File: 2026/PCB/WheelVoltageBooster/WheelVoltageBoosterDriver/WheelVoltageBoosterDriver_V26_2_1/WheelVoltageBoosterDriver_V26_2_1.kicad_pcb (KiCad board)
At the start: 2 copper layers, 100 x 65 mm, 232 parts, among them J1 Conn_01x02_Pin, J10 Conn_01x03_Socket, J11 Conn_01x05_Socket, J13 Conn_01x04_Socket, J2 Conn_01x02_Pin, J3 Conn_01x04_Socket, J4 Conn_01x04_Socket, J5 Conn_01x04_Socket, J6 Conn_01x04_Socket, J7 Conn_01x02_Pin, J8 Conn_01x07_Socket, J9 Conn_01x03_Socket, SW1 SW_MEC_5E, SW2 SW_MEC_5E, U1 MAX3051, U2 LM5170QPHPTQ1, U3 STM32H523CEU6, U4 TMP235AQDCKRQ1, U5 MAX20405AFOA/VY+, U6 MCP1703AT-3302E/CB, U7 MAX20405AFOA/VY+, Y1 Crystal_GND2

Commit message: FTP割り当て完了
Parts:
- removed C100, C101, C102, C103, C104, C105, C106, C107, C60, C61, C62, C80, C81, C82, C83, C84, C85, C86, C87, C88, C89, C90, C91, C92, C93, C94, C95, C96, C97, C98, C99: 10u, Capacitor_SMD:C_1210_3225Metric_Pad1.33x2.70mm_HandSolder
- removed D11, D12, D8: LED, WheelVoltageBooster_LIB_FTP:LED_1608_user_dif
- removed D13, D14: SMAJ26A, WheelVoltageBooster_LIB_FTP:D_SMA_UD
- removed FET11, FET12, FET13, FET14: FDMS86183, WheelVoltageBooster_LIB_FTP:PQFN-8-EP_6x5mm_P1.27mm_Generic_ud
- removed J6: Conn_01x04_Socket, WheelVoltageBooster_LIB_FTP:PinSocket_1x04_P2.54mm_Vertical_ud
- removed R41, R42: 1m, Resistor_SMD:R_2512_6332Metric
- removed R45, R46, R49, R50, R53, R54, R55, R56: 50k, Resistor_SMD:R_0402_1005Metric_Pad0.72x0.64mm_HandSolder
- removed REF** (x4): hole_M3_User, WheelVoltageBooster_LIB_FTP:hole_M3_User
- removed REF** (x4): MountingHole_2.2mm_M2_Pad_Via, MountingHole:MountingHole_2.2mm_M2_Pad_Via
- removed REF**: Symbol_HighVoltage_Triangle_6x6mm_Copper, Symbol:Symbol_HighVoltage_Triangle_6x6mm_Copper
- added R16: 50k, Resistor_SMD:R_0603_1608Metric_Pad0.98x0.95mm_HandSolder, F.Cu at (142.4, 50.9)
- added U10: HIP2101EIBZT, Package_SO:SOIC-8-1EP_3.9x4.9mm_P1.27mm_EP2.514x3.2mm, F.Cu at (141.8, 83.3)
- added U8: MAX15158A, Package_DFN_QFN:TQFN-32-1EP_5x5mm_P0.5mm_EP3.1x3.1mm, F.Cu at (150.3, 83.3)
- added U9: HIP2101EIBZT, Package_SO:SOIC-8-1EP_3.9x4.9mm_P1.27mm_EP2.514x3.2mm, F.Cu at (158.6, 83.1)
- C10: value 10n -> 10u; footprint Capacitor_SMD:C_0603_1608Metric_Pad1.08x0.95mm_HandSolder -> Capacitor_SMD:C_1210_3225Metric_Pad1.33x2.70mm_HandSolder
- C11, C13: value 9n -> 1n
- C16: value 10n -> 68u; footprint Capacitor_SMD:C_0603_1608Metric_Pad1.08x0.95mm_HandSolder -> WheelVoltageBooster_LIB_FTP:CAP_EEEFN1K470UP
- C27, C29, C31: value 220u -> 10u; footprint WheelVoltageBooster_LIB_FTP:CAP_EEEFN1H181UP -> Capacitor_SMD:C_1210_3225Metric_Pad1.33x2.70mm_HandSolder
- C28, C30, C35, C37: value 10u -> 68u; footprint Capacitor_SMD:C_1210_3225Metric_Pad1.33x2.70mm_HandSolder -> WheelVoltageBooster_LIB_FTP:CAP_EEEFN1K470UP; moved to F.Cu
- C3: value 1n -> 2.2u
- C32, C50: value 10u -> 1n; footprint Capacitor_SMD:C_1210_3225Metric_Pad1.33x2.70mm_HandSolder -> Capacitor_SMD:C_0603_1608Metric_Pad1.08x0.95mm_HandSolder
- C33: value 220u -> 68u; footprint WheelVoltageBooster_LIB_FTP:CAP_EEEFN1H181UP -> WheelVoltageBooster_LIB_FTP:CAP_EEEFN1K470UP
- C39: value 220n -> 68u; footprint Capacitor_SMD:C_0603_1608Metric_Pad1.08x0.95mm_HandSolder -> WheelVoltageBooster_LIB_FTP:CAP_EEEFN1K470UP
- C4: value 1n -> 47n
- C40: value 220n -> 10u; footprint Capacitor_SMD:C_0603_1608Metric_Pad1.08x0.95mm_HandSolder -> Capacitor_SMD:C_1210_3225Metric_Pad1.33x2.70mm_HandSolder
- C45, C47, C51, C53: value 68u -> 220u; footprint WheelVoltageBooster_LIB_FTP:CAP_EEEFN1K470UP -> WheelVoltageBooster_LIB_FTP:CAP_EEEFN1H181UP
- C49, C55: value 68u -> 1n; footprint WheelVoltageBooster_LIB_FTP:CAP_EEEFN1K470UP -> Capacitor_SMD:C_0603_1608Metric_Pad1.08x0.95mm_HandSolder
- C5: value 1u -> 73n
- C56, C58: value 10u -> 220u; footprint Capacitor_SMD:C_1210_3225Metric_Pad1.33x2.70mm_HandSolder -> WheelVoltageBooster_LIB_FTP:CAP_EEEFN1H181UP
- C57, C59: value 68u -> 10u; footprint WheelVoltageBooster_LIB_FTP:CAP_EEEFN1K470UP -> Capacitor_SMD:C_1210_3225Metric_Pad1.33x2.70mm_HandSolder
- C6: value 500p -> 73p
- C7: value 500p -> 0.1u
- C8: value 47n -> 0.1u
- C9: value 47n -> 68u; footprint Capacitor_SMD:C_0603_1608Metric_Pad1.08x0.95mm_HandSolder -> WheelVoltageBooster_LIB_FTP:CAP_EEEFN1K470UP
- D1, D2: value SMAJ12A -> LED; footprint WheelVoltageBooster_LIB_FTP:D_SMA_UD -> WheelVoltageBooster_LIB_FTP:LED_1608_user_dif
- J1: value Conn_01x02_Pin -> Conn_01x04_Socket; footprint WheelVoltageBooster_LIB_FTP:AMASS_XT30PW-M_1x02_P2.50mm_Horizontal_ud -> Connector_PinSocket_2.54mm:PinSocket_1x04_P2.54mm_Vertical
- J3, J4, J5: footprint WheelVoltageBooster_LIB_FTP:PinSocket_1x04_P2.54mm_Vertical_ud -> Connector_PinSocket_2.54mm:PinSocket_1x04_P2.54mm_Vertical
- R1: value 2.4k -> 3k; footprint Resistor_SMD:R_0603_1608Metric_Pad0.98x0.95mm_HandSolder -> Resistor_SMD:R_0402_1005Metric_Pad0.72x0.64mm_HandSolder
- R10: value 43k -> 2k; footprint Resistor_SMD:R_0603_1608Metric_Pad0.98x0.95mm_HandSolder -> Resistor_SMD:R_0402_1005Metric_Pad0.72x0.64mm_HandSolder
- R11: value 21k -> 7.2k; footprint Resistor_SMD:R_0603_1608Metric_Pad0.98x0.95mm_HandSolder -> Resistor_SMD:R_0402_1005Metric_Pad0.72x0.64mm_HandSolder
- R14: value 11k -> 50k
- R17: value 11k -> 1k
- R2: value 2.4k -> 1k; footprint Resistor_SMD:R_0603_1608Metric_Pad0.98x0.95mm_HandSolder -> Resistor_SMD:R_0402_1005Metric_Pad0.72x0.64mm_HandSolder
- R3: value 25 -> 3k; footprint Resistor_SMD:R_0603_1608Metric_Pad0.98x0.95mm_HandSolder -> Resistor_SMD:R_0402_1005Metric_Pad0.72x0.64mm_HandSolder
- R31, R32: value 1k -> 10; footprint Resistor_SMD:R_0603_1608Metric_Pad0.98x0.95mm_HandSolder -> Resistor_SMD:R_01005_0402Metric_Pad0.57x0.30mm_HandSolder
- R36: value 50k -> 3m
- R37: value 50k -> 10; footprint Resistor_SMD:R_0603_1608Metric_Pad0.98x0.95mm_HandSolder -> Resistor_SMD:R_01005_0402Metric_Pad0.57x0.30mm_HandSolder
- R38: value 1M -> 10; footprint Resistor_SMD:R_0402_1005Metric_Pad0.72x0.64mm_HandSolder -> Resistor_SMD:R_01005_0402Metric_Pad0.57x0.30mm_HandSolder
- R4: value 24k -> 1k; footprint Resistor_SMD:R_0603_1608Metric_Pad0.98x0.95mm_HandSolder -> Resistor_SMD:R_0402_1005Metric_Pad0.72x0.64mm_HandSolder
- R5: value 24k -> 100k; footprint Resistor_SMD:R_0603_1608Metric_Pad0.98x0.95mm_HandSolder -> Resistor_SMD:R_0402_1005Metric_Pad0.72x0.64mm_HandSolder
- R6: value 10k -> 35k; footprint Resistor_SMD:R_0603_1608Metric_Pad0.98x0.95mm_HandSolder -> Resistor_SMD:R_0402_1005Metric_Pad0.72x0.64mm_HandSolder
- R7: value 10k -> 60k; footprint Resistor_SMD:R_0603_1608Metric_Pad0.98x0.95mm_HandSolder -> Resistor_SMD:R_0402_1005Metric_Pad0.72x0.64mm_HandSolder
- R8: value 10k -> 100k; footprint Resistor_SMD:R_0603_1608Metric_Pad0.98x0.95mm_HandSolder -> Resistor_SMD:R_0402_1005Metric_Pad0.72x0.64mm_HandSolder
- R9: value 65k -> 48k; footprint Resistor_SMD:R_0603_1608Metric_Pad0.98x0.95mm_HandSolder -> Resistor_SMD:R_0402_1005Metric_Pad0.72x0.64mm_HandSolder
- U2: value LM5170QPHPTQ1 -> TMP235AQDCKRQ1; footprint WheelVoltageBooster_LIB_FTP:LM5170QPHPTQ1 -> Package_TO_SOT_SMD:SOT-353_SC-70-5
- Y1: value Crystal_GND2 -> CSTNE16M0V530000R0
- moved C53 58.4 mm to (90.3, 51.6)
- moved C10 57.1 mm to (183.3, 48.0)
- moved C3 57.1 mm to (198.1, 45.7)
- moved C5 57.1 mm to (198.1, 42.7)
- moved C6 57.1 mm to (201.6, 45.7)
- moved C8 57.1 mm to (201.6, 44.2)
- moved R1 57.1 mm to (201.6, 42.7)
- moved R10 57.1 mm to (194.5, 48.0)
- moved R11 57.1 mm to (198.1, 41.2)
- moved R3 57.1 mm to (201.6, 41.2)
- moved R4 57.1 mm to (198.1, 44.2)
- moved C14 57.1 mm to (198.1, 38.1)
- moved C19 57.1 mm to (201.6, 38.1)
- moved C24 57.1 mm to (188.9, 58.3)
- moved D1 57.1 mm to (199.9, 48.3)
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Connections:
- net +6V5 renamed 6V5
- C1 pad 1: +3V3 -> 3V3
- C10 pad 1: GND -> 50V
- C10 pad 2: Net-(U2-SS) -> GND
- C11 pad 1: IOUT1 -> CSP1
- C13 pad 1: IOUT2 -> CSN1
- C14 pad 2: +3V3 -> 3V3
- C15 pad 2: +3V3 -> 3V3
- C16 pad 1: GND -> 50V
- C16 pad 2: Net-(U2-ISETA) -> GND
- C17 pad 2: +3V3 -> 3V3
- C18 pad 2: +3V3 -> 3V3
- C19 pad 2: +3V3 -> 3V3
- C2 pad 1: GND -> 3V3
- C2 pad 2: +10V -> GND
- C20 pad 1: +3V3 -> 3V3
- C22 pad 1: +3V3 -> 3V3
- C24 pad 1: +3V3 -> 3V3
- C27 pad 1: +20V -> 50V
- C28 pad 1: +20V -> 50V
- C29 pad 1: +20V -> 50V
- C3 pad 2: Net-(U2-RAMP1) -> Net-(U8-BIAS)
- C30 pad 1: +20V -> 50V
- C31 pad 1: +20V -> 50V
- C32 pad 1: +20V -> CSP1
- C32 pad 2: GND -> CSN1
- C33 pad 1: +20V -> 50V
- C34 pad 1: +20V -> 50V
- C35 pad 1: +20V -> 50V
- C36 pad 1: +20V -> 50V
- C37 pad 1: +20V -> 50V
- C38 pad 1: +20V -> 50V
- C39 pad 1: /Power_Circuit/SW2 -> 50V
- C39 pad 2: /Power_Circuit/HB2 -> GND
- C4 pad 1: GND -> Net-(U8-SS)
- C4 pad 2: Net-(U2-RAMP2) -> GND
- C40 pad 1: /Power_Circuit/SW1 -> 50V
- C40 pad 2: /Power_Circuit/HB1 -> GND
- C41 pad 1: +50V -> 50V
- C42 pad 1: +50V -> 50V
- C43 pad 1: +50V -> 50V
- C44 pad 1: +50V -> 50V
- C45 pad 1: +50V -> 25V
- C46 pad 1: +20V -> 25V
- C47 pad 1: +50V -> 25V
- C48 pad 1: +20V -> 25V
- C49 pad 1: +50V -> CSP2
- C5 pad 1: GND -> Net-(C5-Pad1)
- C5 pad 2: Net-(U2-OPT) -> GND
- C50 pad 1: +50V -> CSN2
- C51 pad 1: +50V -> 25V
- C52 pad 1: +50V -> 25V
- C53 pad 1: +50V -> 25V
- C54 pad 1: +50V -> 25V
- C55 pad 1: +50V -> CSP2
- C55 pad 2: GND -> CSN2
- C56 pad 1: +50V -> 25V
- C57 pad 1: +50V -> 25V
- C58 pad 1: +50V -> 25V
- C59 pad 1: +50V -> 25V
- C6 pad 1: GND -> COMP
- C6 pad 2: Net-(U2-COMP1) -> GND
- C64 pad 1: +20V -> 25V
- C65 pad 1: +20V -> 25V
- C7 pad 1: GND -> Net-(U9-HB)
- C7 pad 2: Net-(U2-COMP2) -> HS1
- C72 pad 1: +3V3 -> 3V3
- C73 pad 1: +20V -> 25V
- C74 pad 1: +20V -> 25V
- C77 pad 1: +10V -> 10V
- C78 pad 1: +10V -> 10V
- C79 pad 1: +10V -> 10V
- C8 pad 1: Net-(C8-Pad1) -> Net-(U10-HB)
- C8 pad 2: Net-(U2-COMP1) -> HS2
- C9 pad 1: Net-(C9-Pad1) -> 50V
- C9 pad 2: Net-(U2-COMP2) -> GND
- D1 pad 1: /Power_Circuit/HB1 -> GND
- D1 pad 2: +10V -> Net-(D1-A)
- D2 pad 1: /Power_Circuit/HB2 -> GND
- D2 pad 2: +10V -> Net-(D2-A)
- FET10 pad 1: GND -> SR2
- FET10 pad 2: GND -> SR2
- FET10 pad 3: GND -> SR2
- FET10 pad 4: /Power_Circuit/LO1 -> LO2
- FET10 pad 5: /Power_Circuit/SW1 -> HS2
- FET3 pad 1: /Power_Circuit/BRKS -> HS1
- FET3 pad 2: /Power_Circuit/BRKS -> HS1
- FET3 pad 3: /Power_Circuit/BRKS -> HS1
- FET3 pad 4: /Power_Circuit/BRKG -> HO1
- FET3 pad 5: +20V -> 50V
- FET4 pad 1: /Power_Circuit/BRKS -> SR1
- FET4 pad 2: /Power_Circuit/BRKS -> SR1
- FET4 pad 3: /Power_Circuit/BRKS -> SR1
- FET4 pad 4: /Power_Circuit/BRKG -> LO1
- FET4 pad 5: +20V -> HS1
- FET5 pad 1: /Power_Circuit/BRKS -> HS1
- FET5 pad 2: /Power_Circuit/BRKS -> HS1
- FET5 pad 3: /Power_Circuit/BRKS -> HS1
- FET5 pad 4: /Power_Circuit/BRKG -> HO1
- FET5 pad 5: /Power_Circuit/CS1B -> 50V
- FET6 pad 1: /Power_Circuit/BRKS -> SR1
- FET6 pad 2: /Power_Circuit/BRKS -> SR1
- FET6 pad 3: /Power_Circuit/BRKS -> SR1
- FET6 pad 4: /Power_Circuit/BRKG -> LO1
- FET6 pad 5: /Power_Circuit/CS1B -> HS1
- FET7 pad 1: GND -> HS2
- FET7 pad 2: GND -> HS2
- FET7 pad 3: GND -> HS2
- FET7 pad 4: /Power_Circuit/LO2 -> HO2
- FET7 pad 5: /Power_Circuit/SW2 -> 50V
- FET8 pad 1: GND -> SR2
- FET8 pad 2: GND -> SR2
- FET8 pad 3: GND -> SR2
- FET8 pad 4: /Power_Circuit/LO1 -> LO2
- FET8 pad 5: /Power_Circuit/SW1 -> HS2
- FET9 pad 1: GND -> HS2
- FET9 pad 2: GND -> HS2
- FET9 pad 3: GND -> HS2
- FET9 pad 4: /Power_Circuit/LO2 -> HO2
- FET9 pad 5: /Power_Circuit/SW2 -> 50V
- J1 pad 1: GND -> 50V
- J1 pad 2: +20V -> 50V
- J10 pad 1: +3V3 -> 3V3
- J10 pad 2: +3V3 -> 3V3
- J10 pad 3: +3V3 -> 3V3
- J11 pad 2: +20V -> 25V
- J13 pad 2: +20V -> 25V
- J2 pad 1: +20V -> 25V
- J3 pad 1: +50V -> 50V
- J3 pad 2: +50V -> 50V
- J3 pad 3: +50V -> 50V
- J3 pad 4: +50V -> 50V
- J4 pad 1: +50V -> GND
- J4 pad 2: +50V -> GND
- J4 pad 3: +50V -> GND
- J4 pad 4: +50V -> GND
- J7 pad 1: +20V -> 25V
- J8 pad 6: +3V3 -> 3V3
- J9 pad 1: +3V3 -> 3V3
- J9 pad 2: +3V3 -> 3V3
- J9 pad 3: +3V3 -> 3V3
- L1 pad 1: /Power_Circuit/CS2A -> 25V
- L1 pad 2: /Power_Circuit/SW2 -> HS1
- L1 pad 3: GND -> (no net)
- L2 pad 1: /Power_Circuit/CS1A -> 25V
- L2 pad 2: /Power_Circuit/SW1 -> HS2
- L2 pad 3: GND -> (no net)
- L4 pad 2: +10V -> 10V
- R1 pad 1: GND -> LO1
- R1 pad 2: Net-(C8-Pad1) -> DLFB1
- R10 pad 1: GND -> FB
- R10 pad 2: Net-(U2-OVPB) -> GND
- R11 pad 1: GND -> COMP
- R11 pad 2: Net-(U2-IPK) -> Net-(C5-Pad1)
- R14 pad 1: IOUT1 -> 50V
- R14 pad 2: GND -> Net-(D1-A)
- R15 pad 1: +20V -> 25V
- R17 pad 1: IOUT2 -> /Power_Circuit/MREN
- R17 pad 2: GND -> Net-(D7-A)
- R2 pad 1: GND -> DLFB1
- R2 pad 2: Net-(C9-Pad1) -> GND
- R22 pad 1: +50V -> 50V
- R22 pad 2: VM_SCAN2 -> /Power_Circuit/MRVFB1
- R23 pad 1: VM_SCAN2 -> /Power_Circuit/MRVFB1
- R24 pad 1: +50V -> 50V
- R24 pad 2: VM_SCAN1 -> /Power_Circuit/MRVFB2
- R25 pad 1: VM_SCAN1 -> /Power_Circuit/MRVFB2
- R26 pad 1: +3V3 -> 3V3
- R3 pad 1: +10V -> LO2
- R3 pad 2: Net-(U2-OPT) -> DLFB2
- R31 pad 1: EN1 -> CSP1
- R31 pad 2: Net-(D7-A) -> SR1
- R32 pad 1: EN2 -> CSN1
- R32 pad 2: Net-(D8-A) -> GND
- R35 pad 1: +3V3 -> 3V3
- R36 pad 1: +50V -> SR1
- R36 pad 2: Net-(D11-A) -> GND
- R37 pad 1: +50V -> CSP2
- R37 pad 2: Net-(D12-A) -> SR2
- R38 pad 1: /Power_Circuit/BRKG -> CSN2
- R38 pad 2: /Power_Circuit/BRKS -> GND
- R4 pad 1: Net-(U2-VINX) -> DLFB2
- R4 pad 2: Net-(U2-RAMP1) -> GND
- R5 pad 1: Net-(U2-VINX) -> Net-(U8-BIAS)
- R5 pad 2: Net-(U2-RAMP2) -> /Power_Circuit/PGOOD
- R6 pad 2: Net-(U2-OSC) -> Net-(U8-RAMP)
- R61 pad 1: +20V -> 25V
- R62 pad 1: +10V -> 10V
- R64 pad 1: +3V3 -> 3V3
- R68 pad 2: +10V -> 10V
- R7 pad 2: Net-(U2-SYNCOUT) -> Net-(U8-ILIM)
- R8 pad 2: Net-(U2-DT) -> Net-(U8-OVP)
- R9 pad 1: GND -> 50V
- R9 pad 2: Net-(U2-OVPA) -> FB
- U1 pad 3: +3V3 -> 3V3
- U2 pad 1: /Power_Circuit/CS2A -> unconnected-(U2-NC-Pad1)
- U2 pad 2: /Power_Circuit/CS1B -> GND
- U2 pad 3: unconnected-(U2-NC-Pad3) -> TEMP2
- U2 pad 4: Net-(U2-VINX) -> 3V3
- U3 pad 1: +3V3 -> 3V3
- U3 pad 10: VM_SCAN1 -> /Power_Circuit/MREN
- U3 pad 11: VM_SCAN2 -> /Power_Circuit/PGOOD
- U3 pad 12: IOUT2 -> /Power_Circuit/MRVFB1
- U3 pad 13: IOUT1 -> /Power_Circuit/MRVFB2
- U3 pad 14: TEMP_S -> /Power_Circuit/10VEN
- U3 pad 15: DIR -> unconnected-(U3-PA5-Pad15)
- U3 pad 16: EN2 -> TEMP1
- U3 pad 17: ISETD -> TEMP2
- U3 pad 18: UVLO -> unconnected-(U3-PB0-Pad18)
- U3 pad 19: EN1 -> unconnected-(U3-PB1-Pad19)
- U3 pad 24: +3V3 -> 3V3
- U3 pad 36: +3V3 -> 3V3
- U3 pad 48: +3V3 -> 3V3
- U3 pad 9: +3V3 -> 3V3
- U4 pad 3: TEMP_S -> TEMP1
- U4 pad 4: +3V3 -> 3V3
- U5 pad 3: +20V -> 25V
- U5 pad 9: +20V -> 25V
- U6 pad 2: +3V3 -> 3V3
- U7 pad 1: 10VEN -> /Power_Circuit/10VEN
- U7 pad 13: +10V -> 10V
- U7 pad 3: +20V -> 25V
- U7 pad 9: +20V -> 25V
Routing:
- net +20V: track 186.5 -> 0.00 mm, vias 39 -> 0
- net 6V5: track 129.7 -> 0.00 mm, vias 6 -> 0
- net +10V: track 124.5 -> 0.00 mm, vias 8 -> 0
- net +3V3: track 109.3 -> 0.00 mm, vias 3 -> 0
- net FET_FAN: track 96.2 -> 0.00 mm, vias 4 -> 0
- net CANH: track 93.1 -> 0.00 mm, vias 1 -> 0
- net CANL: track 91.4 -> 0.00 mm, vias 1 -> 0
- net GND: track 67.2 -> 0.00 mm, vias 290 -> 0
- net VM_SCAN2: track 62.4 -> 0.00 mm, vias 3 -> 0
- net /Power_Circuit/HO1: track 48.0 -> 0.00 mm, vias 3 -> 0
- net +50V: track 46.9 -> 0.00 mm, vias 62 -> 0
- net /Power_Circuit/HO2: track 44.4 -> 0.00 mm, vias 3 -> 0
- net VM_SCAN1: track 44.1 -> 0.00 mm, vias 3 -> 0
- net 10VEN: track 40.1 -> 0.00 mm, vias 2 -> 0
- net /Power_Circuit/BRKG: track 39.9 -> 0.00 mm, vias 5 -> 0
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- removed copper zone on B.Cu, net +20V
- removed copper zone on F.Cu, net +20V
- removed copper zone on B.Cu, net +3V3
- removed copper zone on F.Cu, net +3V3
- removed copper zone on B.Cu, net +50V
- removed copper zone on F.Cu, net +50V
- removed copper zone on F.Cu, net /Power_Circuit/BRKS
- removed copper zone on F.Cu, net /Power_Circuit/CS1A
- removed copper zone on F.Cu, net /Power_Circuit/CS1B
- removed copper zone on F.Cu, net /Power_Circuit/CS2A
- removed copper zone on F.Cu, net /Power_Circuit/SW1
- removed copper zone on F.Cu, net /Power_Circuit/SW2
- removed copper zone on B.Cu, net GND
- removed copper zone on F.Cu, net GND

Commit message: PCB60%完了
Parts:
- added C60: 10u, Capacitor_SMD:C_1210_3225Metric_Pad1.33x2.70mm_HandSolder, F.Cu at (124.2, 120.9)
- added C61: 10u, Capacitor_SMD:C_1210_3225Metric_Pad1.33x2.70mm_HandSolder, F.Cu at (124.2, 117.6)
- added C62: 10u, Capacitor_SMD:C_1210_3225Metric_Pad1.33x2.70mm_HandSolder, F.Cu at (137.3, 83.3)
- added C80: 10u, Capacitor_SMD:C_1210_3225Metric_Pad1.33x2.70mm_HandSolder, F.Cu at (162.7, 83.3)
- added J6: Conn_01x02_Pin, WheelVoltageBooster_LIB_FTP:AMASS_XT30PW-M_1x02_P2.50mm_Horizontal_ud, F.Cu at (147.5, 113.7)
- added R39: 3m, Resistor_SMD:R_2512_6332Metric, B.Cu at (165.4, 103.3)
- added REF**: MountingHole_2.2mm_M2_Pad_Via, MountingHole:MountingHole_2.2mm_M2_Pad_Via, F.Cu at (110.0, 65.5)
- added REF**: MountingHole_2.2mm_M2_Pad_Via, MountingHole:MountingHole_2.2mm_M2_Pad_Via, F.Cu at (189.5, 124.5)
- added REF**: hole_M3_User, WheelVoltageBooster_LIB_FTP:hole_M3_User, F.Cu at (197.0, 65.5)
- added REF**: MountingHole_2.2mm_M2_Pad_Via, MountingHole:MountingHole_2.2mm_M2_Pad_Via, F.Cu at (190.0, 65.5)
- added REF**: MountingHole_2.2mm_M2_Pad_Via, MountingHole:MountingHole_2.2mm_M2_Pad_Via, F.Cu at (110.0, 124.5)
- added REF**: hole_M3_User, WheelVoltageBooster_LIB_FTP:hole_M3_User, F.Cu at (103.0, 65.5)
- added REF**: hole_M3_User, WheelVoltageBooster_LIB_FTP:hole_M3_User, F.Cu at (197.0, 124.5)
- added REF**: hole_M3_User, WheelVoltageBooster_LIB_FTP:hole_M3_User, F.Cu at (103.0, 124.5)
- C2, J1, U2: moved to B.Cu
- C32, C34, C36, C38, C46, C48, C52, C54, C56: moved to F.Cu
- R1, R10, R11, R2, R3, R4, R5, R6, R7, R8, R9: footprint Resistor_SMD:R_0402_1005Metric_Pad0.72x0.64mm_HandSolder -> Resistor_SMD:R_0603_1608Metric_Pad0.98x0.95mm_HandSolder
- R22, R23, R24, R25: footprint Resistor_SMD:R_0603_1608Metric_Pad0.98x0.95mm_HandSolder -> Resistor_SMD:R_0402_1005Metric_Pad0.72x0.64mm_HandSolder; moved to F.Cu
- R31, R32, R37: footprint Resistor_SMD:R_01005_0402Metric_Pad0.57x0.30mm_HandSolder -> Resistor_SMD:R_0603_1608Metric_Pad0.98x0.95mm_HandSolder
- R36: footprint Resistor_SMD:R_0603_1608Metric_Pad0.98x0.95mm_HandSolder -> Resistor_SMD:R_2512_6332Metric; moved to B.Cu
- R38: footprint Resistor_SMD:R_01005_0402Metric_Pad0.57x0.30mm_HandSolder -> Resistor_SMD:R_0603_1608Metric_Pad0.98x0.95mm_HandSolder; moved to F.Cu
- U8: footprint Package_DFN_QFN:TQFN-32-1EP_5x5mm_P0.5mm_EP3.1x3.1mm -> Package_DFN_QFN:TQFN-32-1EP_5x5mm_P0.5mm_EP3.1x3.1mm_ThermalVias
- moved C40 101.9 mm to (119.1, 120.9), turned to 0 degrees
- moved C10 92.2 mm to (119.1, 114.3)
- moved C53 91.9 mm to (165.0, 105.2), turned to 0 degrees
- moved D2 83.8 mm to (128.7, 116.1)
- moved U2 83.7 mm to (123.7, 96.5), turned to -90 degrees
- moved C2 82.6 mm to (123.7, 98.9), turned to 180 degrees
- moved C47 78.4 mm to (135.0, 105.2), turned to 180 degrees
- moved C58 77.6 mm to (135.0, 114.0), turned to 180 degrees
- moved FET7 77.5 mm to (183.8, 109.6), turned to 0 degrees
- moved C57 76.5 mm to (162.7, 89.9)
- moved C48 75.8 mm to (137.3, 86.6)
- moved R31 75.6 mm to (143.1, 91.4), turned to -90 degrees
- moved R1 73.8 mm to (142.9, 87.4), turned to 0 degrees
- moved D1 73.6 mm to (171.3, 116.1)
- moved D7 72.9 mm to (142.9, 82.8), turned to 0 degrees
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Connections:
- U3 pad 27: USART1_RX -> USART1_TX
- U3 pad 28: USART1_TX -> USART1_RX
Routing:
- net 25V: track 0.00 -> 65.2 mm, vias 0 -> 7
- net 3V3: track 0.00 -> 45.1 mm
- net 6V5: track 0.00 -> 32.5 mm, vias 0 -> 3
- net USART1_TX: track 0.00 -> 25.2 mm, vias 0 -> 2
- net GND: track 0.00 -> 24.3 mm
- net 10V: track 0.00 -> 24.2 mm, vias 0 -> 2
- net SWDIO: track 0.00 -> 23.2 mm, vias 0 -> 2
- net SWCLK: track 0.00 -> 22.8 mm, vias 0 -> 2
- net nRST: track 0.00 -> 20.7 mm
- net HS1: track 0.00 -> 18.4 mm, vias 0 -> 2
- net USART1_RX: track 0.00 -> 18.3 mm, vias 0 -> 1
- net USW: track 0.00 -> 16.7 mm, vias 0 -> 2
- net HS2: track 0.00 -> 16.6 mm, vias 0 -> 2
- net CAN1_TX: track 0.00 -> 14.3 mm, vias 0 -> 2
- net Net-(U8-DH1): track 0.00 -> 13.0 mm, vias 0 -> 2
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- added copper zone on F.Cu, net 25V
- added copper zone on F.Cu, net 50V
- added copper zone on F.Cu, net GND
- added copper zone on F.Cu, net HS1
- added copper zone on F.Cu, net HS2
- added copper zone on F.Cu, net SR1
- added copper zone on F.Cu, net SR2

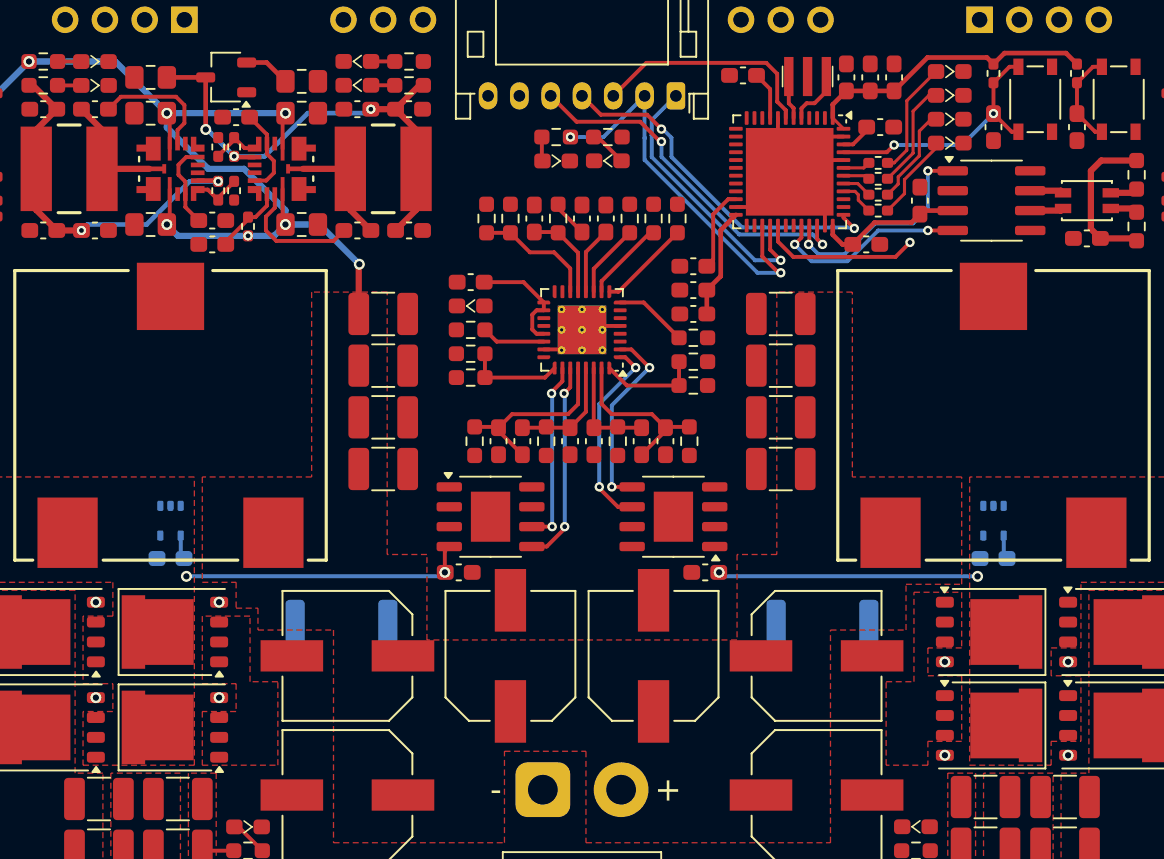
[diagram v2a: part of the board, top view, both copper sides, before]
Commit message: 配線追加
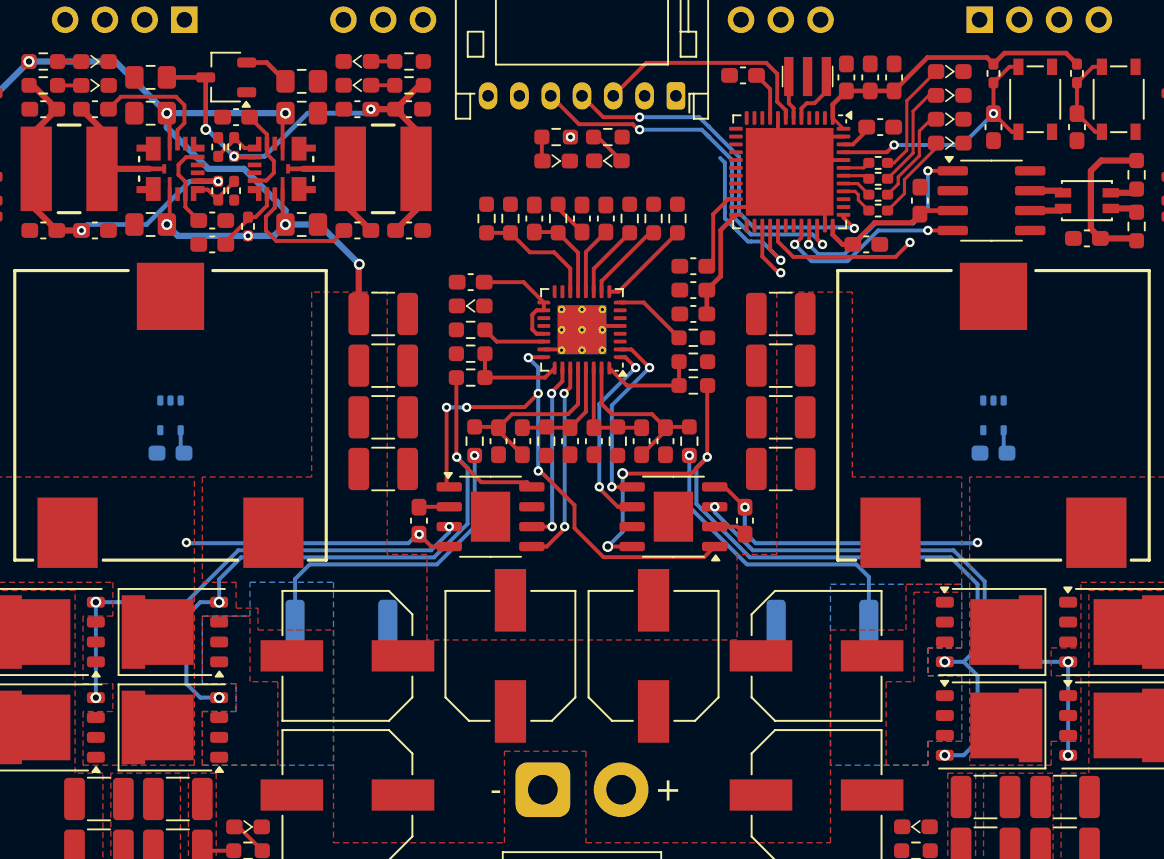
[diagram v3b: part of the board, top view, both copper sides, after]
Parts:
- moved C2 6.73 mm to (123.7, 92.2)
- moved C24 6.73 mm to (176.3, 92.2)
- moved U2 6.73 mm to (123.7, 89.8)
- moved U4 6.73 mm to (176.3, 89.8)
- moved C7 4.17 mm to (139.6, 96.5), turned to -90 degrees
- moved C8 4.17 mm to (160.4, 96.5), turned to 90 degrees
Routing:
- net LO2: track 0.00 -> 54.9 mm, vias 2 -> 5
- net LO1: track 0.00 -> 43.3 mm, vias 2 -> 3
- net HO2: track 0.00 -> 35.3 mm, vias 2 -> 3
- net 10V: track 24.2 -> 58.8 mm, vias 2 -> 7
- net HO1: track 0.00 -> 30.9 mm, vias 2 -> 3
- net USART1_TX: track 25.2 -> 3.59 mm
- net SR1: track 0.00 -> 20.4 mm, vias 0 -> 1
- net SR2: track 0.00 -> 19.7 mm, vias 0 -> 1
- net USART1_RX: track 18.3 -> 11.5 mm
- net HS2: track 16.6 -> 19.3 mm
- net Net-(U10-HB): track 0.00 -> 2.13 mm
- net Net-(U9-HB): track 0.00 -> 1.95 mm
- net SWDIO: track 23.2 -> 25.0 mm
- net SWCLK: track 22.8 -> 24.1 mm
- net HS1: track 18.4 -> 17.4 mm
- added copper zone on B.Cu, net SR1
- added copper zone on B.Cu, net SR2

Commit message: 整合性修正
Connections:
- U3 pad 21: 10VEN -> unconnected-(U3-PB10-Pad21)
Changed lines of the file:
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@@
 	(net 101 "CAN1_TX")
 	(net 102 "Net-(U3-PH1-OSC_OUT)")
-	(net 103 "10VEN")
+	(net 103 "unconnected-(U3-PB10-Pad21)")
 	(net 104 "unconnected-(U3-PB13-Pad26)")
 	(net 105 "unconnected-(U3-PB12-Pad25)")
@@
 			(layers "F.Cu" "F.Mask" "F.Paste")
 			(roundrect_rratio 0.25)
-			(net 103 "10VEN")
+			(net 103 "unconnected-(U3-PB10-Pad21)")
 			(pinfunction "PB10")
-			(pintype "bidirectional")
+			(pintype "bidirectional+no_connect")
 		)
 		(pad "22" smd roundrect

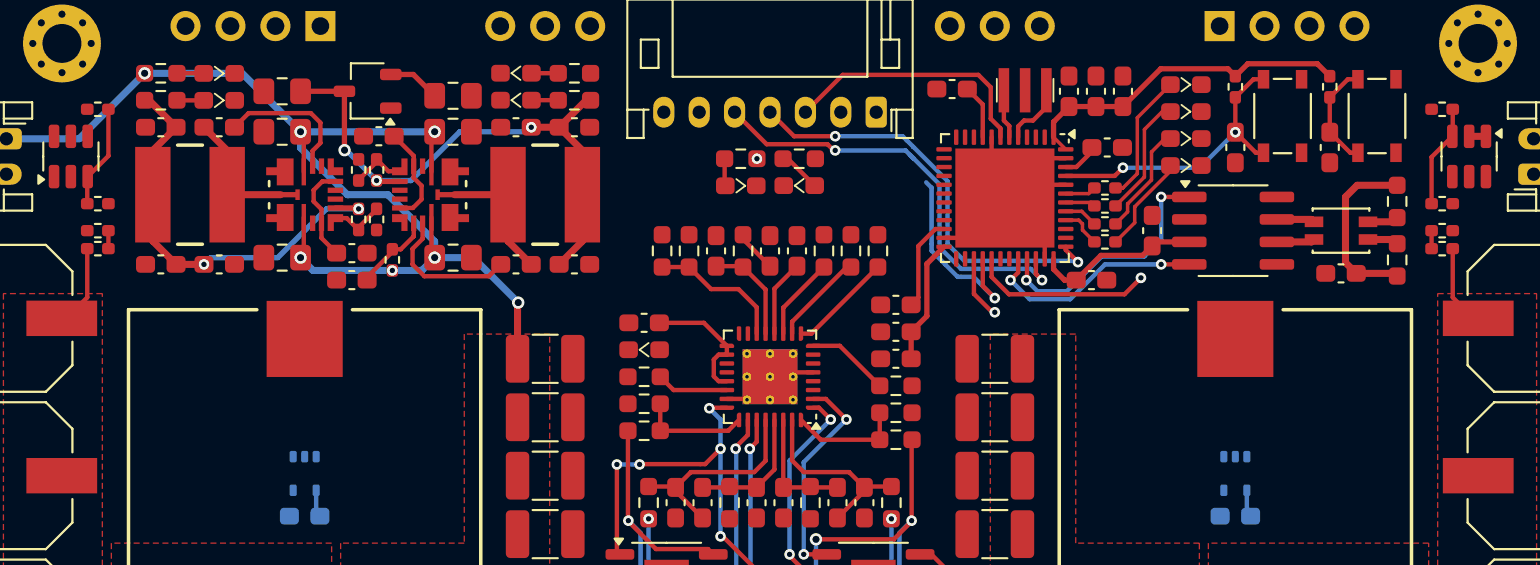
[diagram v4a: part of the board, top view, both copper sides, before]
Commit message: BIAS電源以外の配線完了
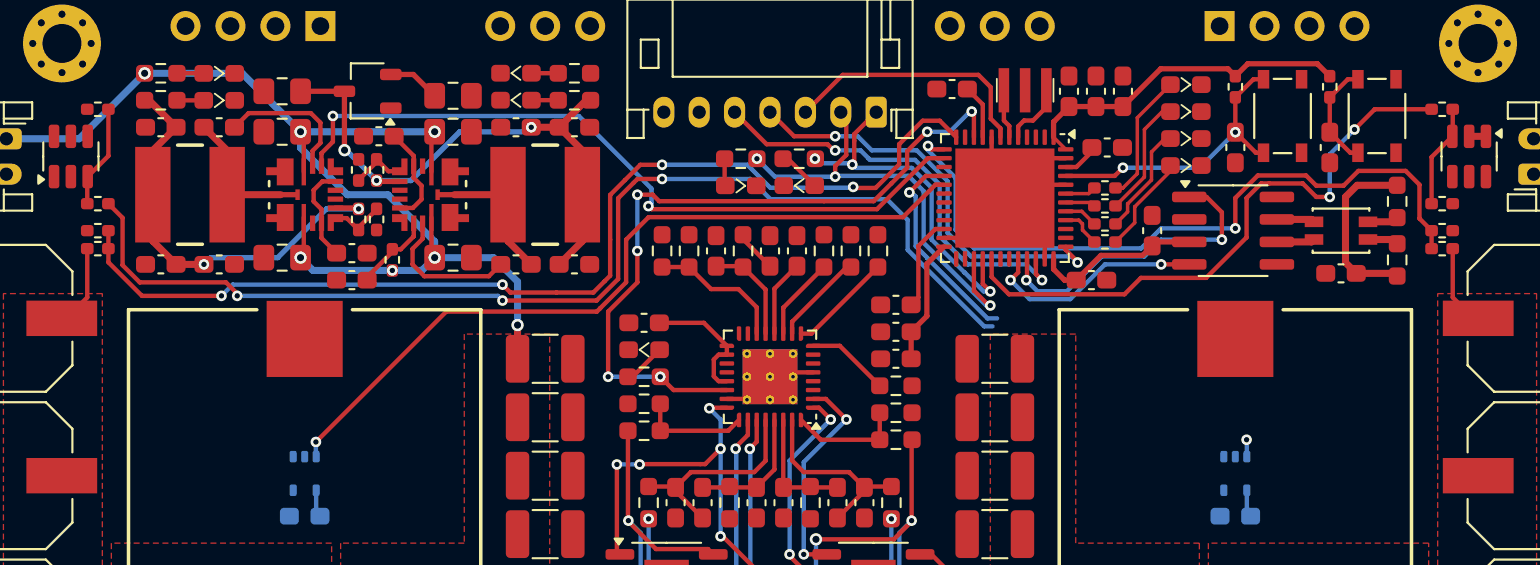
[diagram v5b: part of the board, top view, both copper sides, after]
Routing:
- net FET_FAN: track 10.2 -> 97.8 mm, vias 1 -> 5
- net /Power_Circuit/MRVFB1: track 1.02 -> 59.8 mm, vias 0 -> 4
- net TEMP2: track 0.00 -> 43.8 mm, vias 0 -> 1
- net /Power_Circuit/10VEN: track 0.00 -> 41.8 mm, vias 0 -> 2
- net /Power_Circuit/MRVFB2: track 1.02 -> 40.6 mm, vias 0 -> 2
- net /Power_Circuit/MREN: track 4.07 -> 41.2 mm, vias 0 -> 6
- net USART1_TX: track 3.59 -> 25.5 mm, vias 2 -> 3
- net TEMP1: track 0.00 -> 12.9 mm, vias 0 -> 2
- net USART1_RX: track 11.5 -> 20.6 mm, vias 1 -> 3
- net CAN1_TX: track 14.3 -> 17.5 mm
- net Net-(D7-A): track 0.00 -> 2.42 mm
- net SWDIO: track 25.0 -> 24.4 mm
- net 25V: track 65.2 -> 65.9 mm
